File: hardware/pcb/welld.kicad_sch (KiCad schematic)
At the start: 0 parts

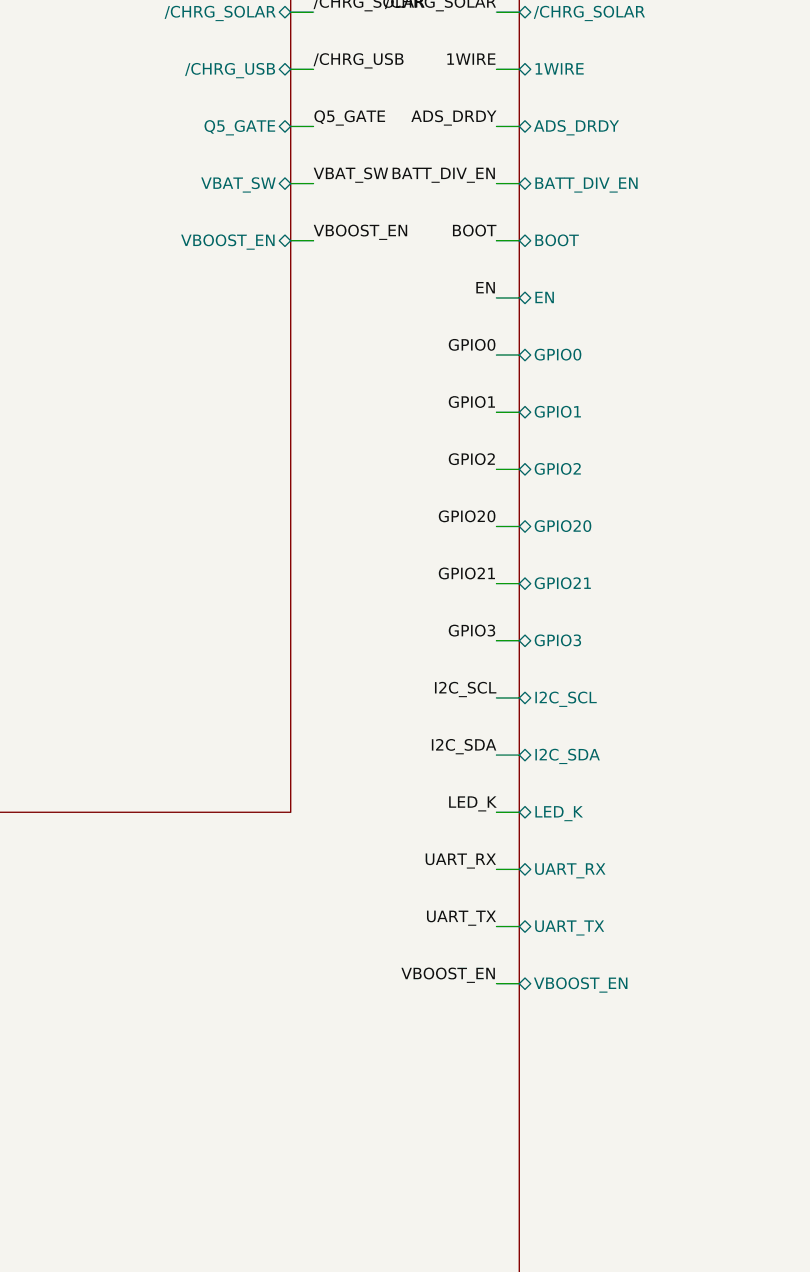
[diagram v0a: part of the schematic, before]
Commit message: hw+fw: wire USB-C to native USB (console/programming); DRDY→GPIO22, reset→GPIO23
User-approved enhancement: the USB-C data lines (previously dead-ended at
the U11 USBLC6 ESD clamp — power-only port) now route through to the ESP32
native USB pins, so the same USB-C used for charging also gives serial
console + programming + USB-DFU.

Schematic:
- USB_DM: U11.6 (I/O1', device side) -> ESP32 GPIO12 (USB D-)
- USB_DP: U11.4 (I/O2', device side) -> ESP32 GPIO13 (USB D+)
  (USBLC6 pins 1&6 = I/O1 net, 3&4 = I/O2 net; device-side pins were NC)
- Added GPIO22/GPIO23 pins to the ESP32 lib symbol (all 4 sheet caches).
- ADS_DRDY moved GPIO12 -> GPIO22, FACTORY_RESET GPIO13 -> GPIO23 (both
  clean pins: no strap, no USB, no JTAG). U11.4/U11.6 removed from NC.
- netlist_check: 393 pins / 75 nets / 10 NC / zero mismatches.

Firmware: WELLD_ADS1115_DRDY_GPIO 12->22, WELLD_FACTORY_RESET_GPIO 13->23
(ranges 0..23), sdkconfig, stub, source comments; PROJECT_VER -> 1.1.3.
Docs: net->pin table (enhancement now APPLIED), CLAUDE/README GPIO tables +
Kconfig tables + USB-C description, schematic_connections USB/DRDY/reset
sections + NC list, firmware-engineer agent brief, CHANGELOG. Host + z2m
tests green.

Co-Authored-By: Claude Opus 4.8 <noreply@anthropic.com>
Claude-Session: https://claude.ai/code/session_01VtMFY5Q94iYbsNPpLcPJyK
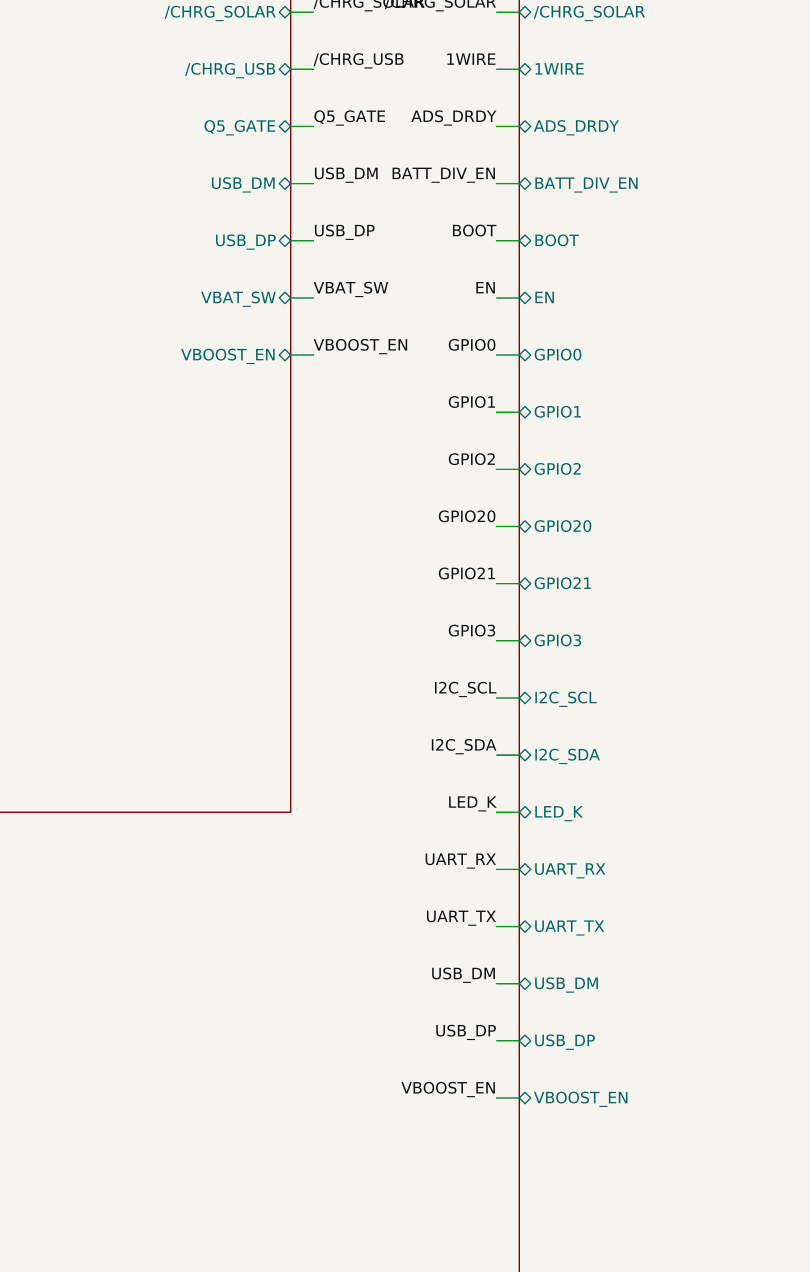
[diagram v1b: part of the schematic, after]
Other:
- sheet mcu ports: added USB_DM, USB_DP; removed none
- sheet power ports: added USB_DM, USB_DP; removed none
